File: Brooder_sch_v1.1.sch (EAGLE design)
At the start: 30 parts, among them J1 DCJ0202, J2 1X2-3.5MM, J3 DCJ0202, J4 1X2-3.5MM, U1 328P

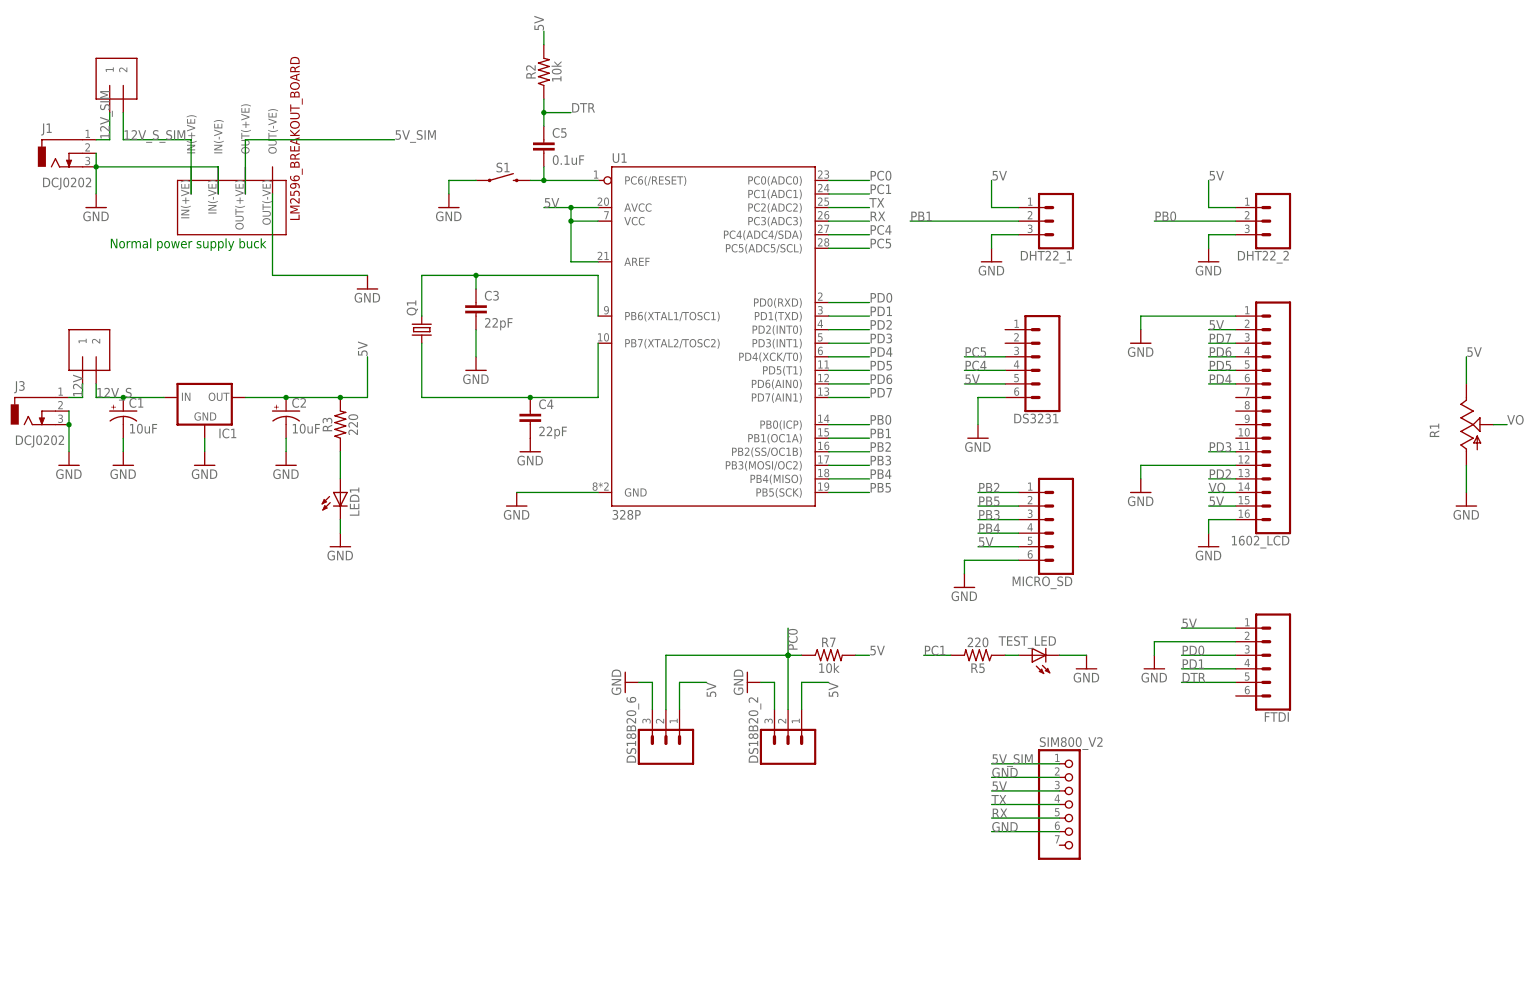
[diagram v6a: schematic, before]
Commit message: Adds ICSP header
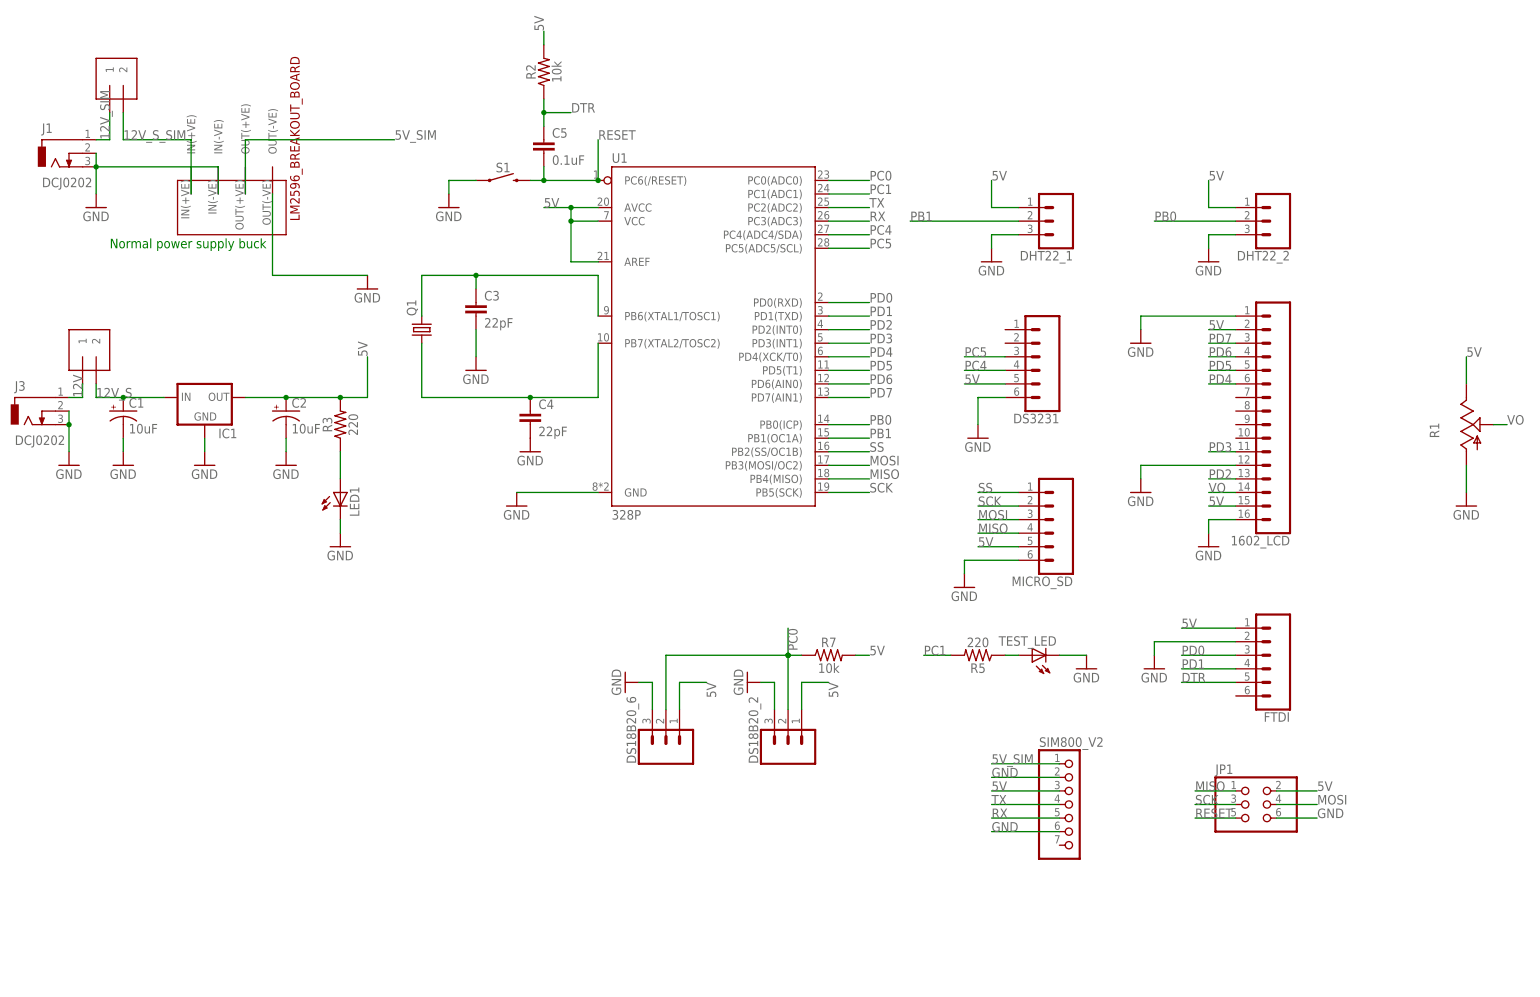
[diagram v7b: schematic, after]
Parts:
- added JP1: (no value), pinhead:PINHD-2X3
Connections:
- net PB2 renamed SS
- removed net N$4: C5.2, S1.2, U1.PC6(/RESET)
- removed net PB3: MICRO_SD.3, U1.PB3(MOSI/OC2)
- removed net PB4: MICRO_SD.4, U1.PB4(MISO)
- removed net PB5: MICRO_SD.2, U1.PB5(SCK)
- new net MISO: JP1.1, MICRO_SD.4, U1.PB4(MISO)
- new net MOSI: JP1.4, MICRO_SD.3, U1.PB3(MOSI/OC2)
- new net RESET: C5.2, JP1.5, S1.2, U1.PC6(/RESET)
- new net SCK: JP1.3, MICRO_SD.2, U1.PB5(SCK)
- net 5V: now also JP1.2
- net GND: now also JP1.6
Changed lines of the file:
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@@
 <part name="R1" library="pot" library_urn="urn:adsk.eagle:library:331" deviceset="TRIM_US-" device="CT6" package3d_urn="urn:adsk.eagle:package:22692/1"/>
 <part name="GND21" library="supply1" library_urn="urn:adsk.eagle:library:371" deviceset="GND" device=""/>
+<part name="JP1" library="pinhead" library_urn="urn:adsk.eagle:library:325" deviceset="PINHD-2X3" device="" package3d_urn="urn:adsk.eagle:package:22462/2"/>
 </parts>
 <sheets>
@@
 <attribute name="VALUE" x="193.04" y="40.64" size="1.778" layer="96"/>
 </instance>
+<instance part="JP1" gate="A" x="154.94" y="-12.7"/>
 </instances>
 <busses>
@@
 <wire x1="195.58" y1="50.8" x2="195.58" y2="45.72" width="0.1524" layer="91"/>
 <pinref part="GND21" gate="1" pin="GND"/>
+</segment>
+<segment>
+<pinref part="JP1" gate="A" pin="6"/>
+<wire x1="160.02" y1="-15.24" x2="167.64" y2="-15.24" width="0.1524" layer="91"/>
+<label x="167.64" y="-15.24" size="1.778" layer="95"/>
 </segment>
 </net>
@@
 <label x="195.58" y="71.12" size="1.778" layer="95"/>
 </segment>
-</net>
-<net name="N$4" class="0">
-<segment>
-<pinref part="S1" gate="G$1" pin="2"/>
-<pinref part="U1" gate="U1" pin="PC6(/RESET)"/>
-<wire x1="20.32" y1="104.14" x2="22.86" y2="104.14" width="0.1524" layer="91"/>
-<pinref part="C5" gate="G$1" pin="2"/>
-<wire x1="22.86" y1="104.14" x2="33.02" y2="104.14" width="0.1524" layer="91"/>
-<wire x1="22.86" y1="106.68" x2="22.86" y2="104.14" width="0.1524" layer="91"/>
-<junction x="22.86" y="104.14"/>
+<segment>
+<pinref part="JP1" gate="A" pin="2"/>
+<wire x1="160.02" y1="-10.16" x2="167.64" y2="-10.16" width="0.1524" layer="91"/>
+<label x="167.64" y="-10.16" size="1.778" layer="95"/>
 </segment>
 </net>
@@
 <wire x1="111.76" y1="96.52" x2="91.44" y2="96.52" width="0.1524" layer="91"/>
 <label x="91.44" y="96.52" size="1.778" layer="95"/>
-</segment>
-</net>
-<net name="PB4" class="0">
-<segment>
-<pinref part="MICRO_SD" gate="G$1" pin="4"/>
-<wire x1="111.76" y1="38.1" x2="104.14" y2="38.1" width="0.1524" layer="91"/>
-<label x="104.14" y="38.1" size="1.778" layer="95"/>
-</segment>
-<segment>
-<pinref part="U1" gate="U1" pin="PB4(MISO)"/>
-<wire x1="76.2" y1="48.26" x2="83.82" y2="48.26" width="0.1524" layer="91"/>
-<label x="83.82" y="48.26" size="1.778" layer="95"/>
-</segment>
-</net>
-<net name="PB3" class="0">
-<segment>
-<pinref part="MICRO_SD" gate="G$1" pin="3"/>
-<wire x1="111.76" y1="40.64" x2="104.14" y2="40.64" width="0.1524" layer="91"/>
-<label x="104.14" y="40.64" size="1.778" layer="95"/>
-</segment>
-<segment>
-<pinref part="U1" gate="U1" pin="PB3(MOSI/OC2)"/>
-<wire x1="76.2" y1="50.8" x2="83.82" y2="50.8" width="0.1524" layer="91"/>
-<label x="83.82" y="50.8" size="1.778" layer="95"/>
-</segment>
-</net>
-<net name="PB5" class="0">
-<segment>
-<pinref part="MICRO_SD" gate="G$1" pin="2"/>
-<wire x1="111.76" y1="43.18" x2="104.14" y2="43.18" width="0.1524" layer="91"/>
-<label x="104.14" y="43.18" size="1.778" layer="95"/>
-</segment>
-<segment>
-<pinref part="U1" gate="U1" pin="PB5(SCK)"/>
-<wire x1="76.2" y1="45.72" x2="83.82" y2="45.72" width="0.1524" layer="91"/>
-<label x="83.82" y="45.72" size="1.778" layer="95"/>
 </segment>
 </net>
@@
 </segment>
 </net>
-<net name="PB2" class="0">
-<segment>
-<pinref part="U1" gate="U1" pin="PB2(SS/OC1B)"/>
-<wire x1="76.2" y1="53.34" x2="83.82" y2="53.34" width="0.1524" layer="91"/>
-<label x="83.82" y="53.34" size="1.778" layer="95"/>
-</segment>
-<segment>
-<pinref part="MICRO_SD" gate="G$1" pin="1"/>
-<wire x1="111.76" y1="45.72" x2="104.14" y2="45.72" width="0.1524" layer="91"/>
-<label x="104.14" y="45.72" size="1.778" layer="95"/>
-</segment>
-</net>
 <net name="12V_S" class="0">
 <segment>
@@
 </segment>
 </net>
+<net name="RESET" class="0">
+<segment>
+<pinref part="JP1" gate="A" pin="5"/>
+<wire x1="152.4" y1="-15.24" x2="144.78" y2="-15.24" width="0.1524" layer="91"/>
+<label x="144.78" y="-15.24" size="1.778" layer="95"/>
+</segment>
+<segment>
+<pinref part="S1" gate="G$1" pin="2"/>
+<pinref part="U1" gate="U1" pin="PC6(/RESET)"/>
+<wire x1="20.32" y1="104.14" x2="22.86" y2="104.14" width="0.1524" layer="91"/>
+<pinref part="C5" gate="G$1" pin="2"/>
+<wire x1="22.86" y1="104.14" x2="33.02" y2="104.14" width="0.1524" layer="91"/>
+<wire x1="22.86" y1="106.68" x2="22.86" y2="104.14" width="0.1524" layer="91"/>
+<junction x="22.86" y="104.14"/>
+<wire x1="33.02" y1="104.14" x2="33.02" y2="111.76" width="0.1524" layer="91"/>
+<junction x="33.02" y="104.14"/>
+<label x="33.02" y="111.76" size="1.778" layer="95"/>
+</segment>
+</net>
+<net name="MISO" class="0">
+<segment>
+<pinref part="U1" gate="U1" pin="PB4(MISO)"/>
+<wire x1="76.2" y1="48.26" x2="83.82" y2="48.26" width="0.1524" layer="91"/>
+<label x="83.82" y="48.26" size="1.778" layer="95"/>
+</segment>
+<segment>
+<pinref part="MICRO_SD" gate="G$1" pin="4"/>
+<wire x1="111.76" y1="38.1" x2="104.14" y2="38.1" width="0.1524" layer="91"/>
+<label x="104.14" y="38.1" size="1.778" layer="95"/>
+</segment>
+<segment>
+<pinref part="JP1" gate="A" pin="1"/>
+<wire x1="152.4" y1="-10.16" x2="144.78" y2="-10.16" width="0.1524" layer="91"/>
+<label x="144.78" y="-10.16" size="1.778" layer="95"/>
+</segment>
+</net>
+<net name="SCK" class="0">
+<segment>
+<pinref part="U1" gate="U1" pin="PB5(SCK)"/>
+<wire x1="76.2" y1="45.72" x2="83.82" y2="45.72" width="0.1524" layer="91"/>
+<label x="83.82" y="45.72" size="1.778" layer="95"/>
+</segment>
+<segment>
+<pinref part="MICRO_SD" gate="G$1" pin="2"/>
+<wire x1="111.76" y1="43.18" x2="104.14" y2="43.18" width="0.1524" layer="91"/>
+<label x="104.14" y="43.18" size="1.778" layer="95"/>
+</segment>
+<segment>
+<pinref part="JP1" gate="A" pin="3"/>
+<wire x1="152.4" y1="-12.7" x2="144.78" y2="-12.7" width="0.1524" layer="91"/>
+<label x="144.78" y="-12.7" size="1.778" layer="95"/>
+</segment>
+</net>
+<net name="MOSI" class="0">
+<segment>
+<pinref part="U1" gate="U1" pin="PB3(MOSI/OC2)"/>
+<wire x1="76.2" y1="50.8" x2="83.82" y2="50.8" width="0.1524" layer="91"/>
+<label x="83.82" y="50.8" size="1.778" layer="95"/>
+</segment>
+<segment>
+<pinref part="MICRO_SD" gate="G$1" pin="3"/>
+<wire x1="111.76" y1="40.64" x2="104.14" y2="40.64" width="0.1524" layer="91"/>
+<label x="104.14" y="40.64" size="1.778" layer="95"/>
+</segment>
+<segment>
+<pinref part="JP1" gate="A" pin="4"/>
+<wire x1="160.02" y1="-12.7" x2="167.64" y2="-12.7" width="0.1524" layer="91"/>
+<label x="167.64" y="-12.7" size="1.778" layer="95"/>
+</segment>
+</net>
+<net name="SS" class="0">
+<segment>
+<pinref part="U1" gate="U1" pin="PB2(SS/OC1B)"/>
+<wire x1="76.2" y1="53.34" x2="83.82" y2="53.34" width="0.1524" layer="91"/>
+<label x="83.82" y="53.34" size="1.778" layer="95"/>
+</segment>
+<segment>
+<pinref part="MICRO_SD" gate="G$1" pin="1"/>
+<wire x1="111.76" y1="45.72" x2="104.14" y2="45.72" width="0.1524" layer="91"/>
+<label x="104.14" y="45.72" size="1.778" layer="95"/>
+</segment>
+</net>
